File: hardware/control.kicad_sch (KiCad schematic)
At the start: 9 parts

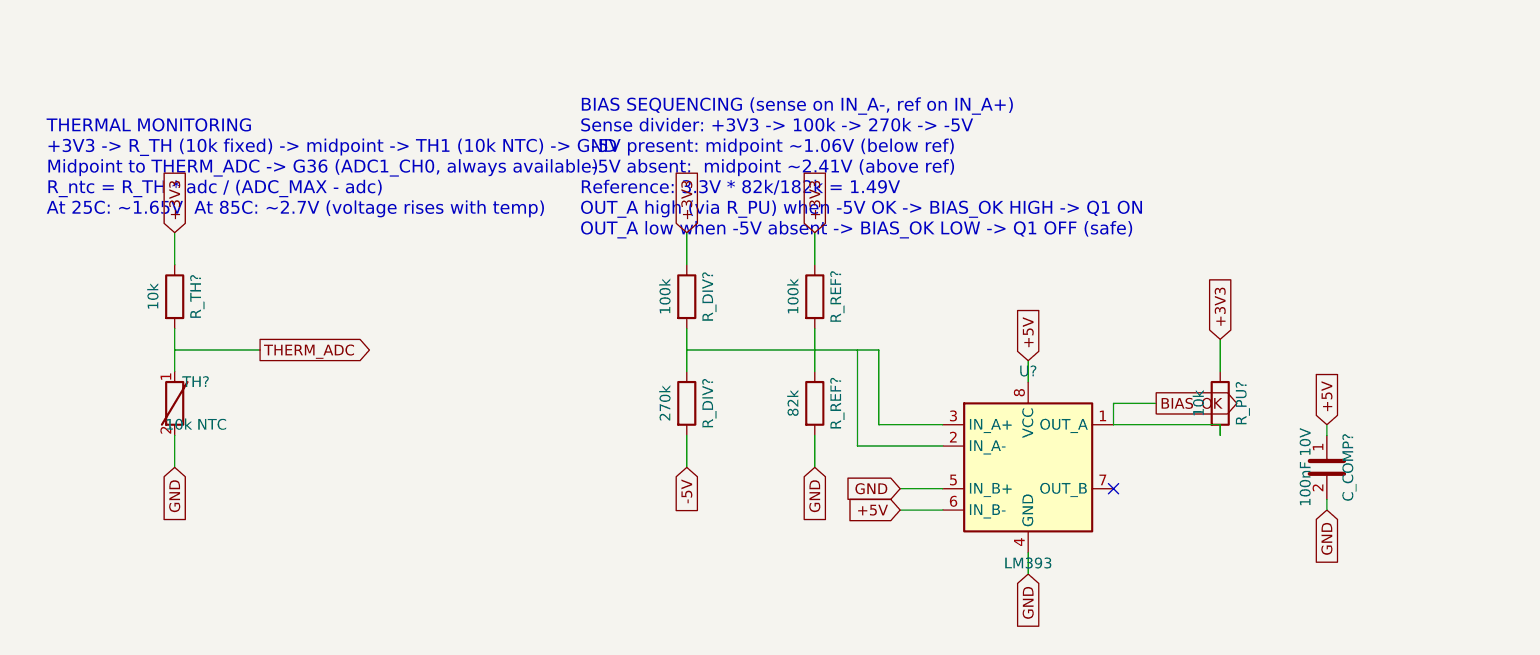
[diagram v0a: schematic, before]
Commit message: jamrf-v2: Add U3V70F15 WiFi PA regulator, FR408HR stackup, full firmware, custom footprints
- Add U3V70F15 buck-boost converter to limit WiFi PA supply to 15V (fixes ZVE-3W-83+ overvoltage)
- Update PCB stackup to Isola FR408HR (Er=3.65, tan d=0.0095) with corrected 0.40mm 50-ohm traces
- Add full operational firmware (main.py): chaos modulation engine, ST7789 display, mode control
- Add 6 custom footprints: M5StickC, Pololu D24V10F5/U3V70F15, Mini-Circuits, Wurth shield, isolator
- Add fp-lib-table and sym-lib-table for custom libraries
- Update README with logo, badges, TIIUAE disclaimer, corrected specs
- Update LICENSE with proper attribution

Co-Authored-By: Claude Opus 4.6 <noreply@anthropic.com>
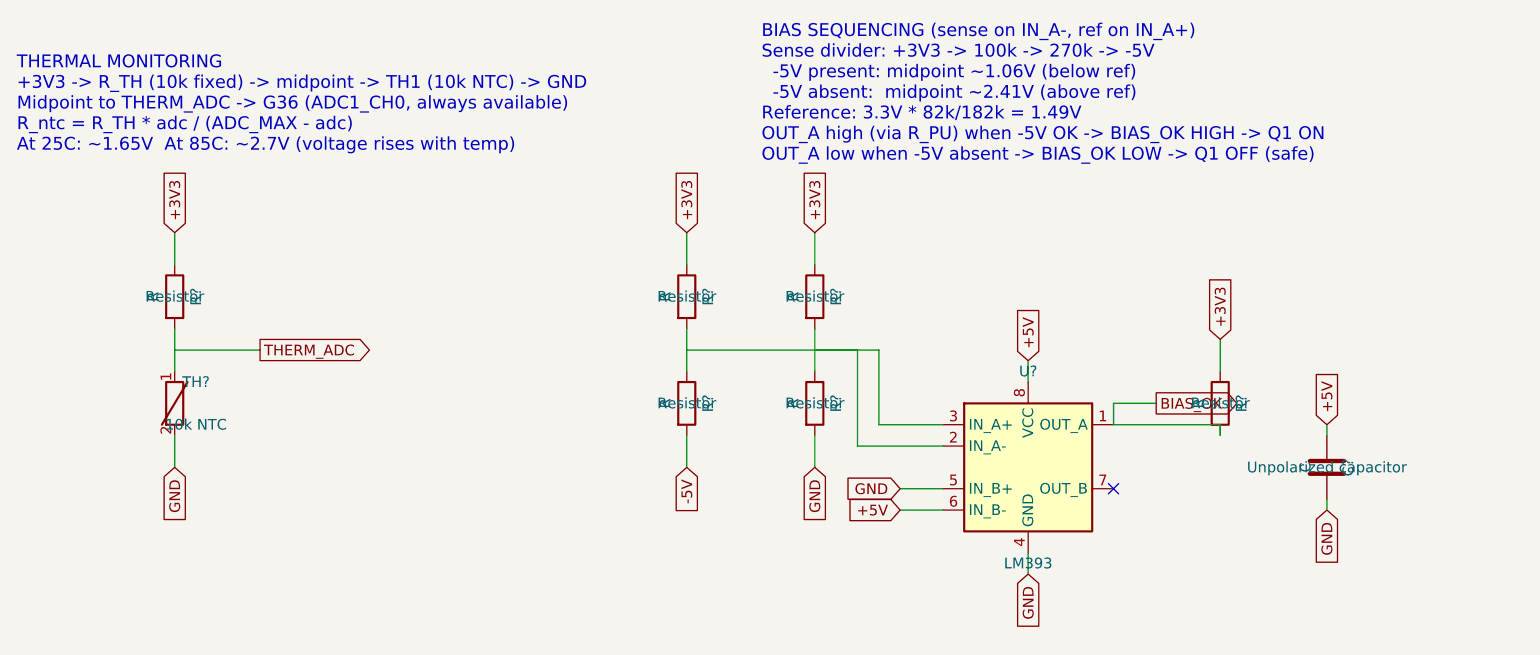
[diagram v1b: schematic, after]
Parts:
- C?: renamed from C_COMP?; value 100nF 10V -> C
- R?: renamed from R_TH?; value 10k -> R
- R?: renamed from R_DIV?; value 100k -> R
- R?: renamed from R_DIV?; value 270k -> R
- R?: renamed from R_REF?; value 100k -> R
- R?: renamed from R_REF?; value 82k -> R
- R?: renamed from R_PU?; value 10k -> R
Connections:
- net at U?.2 (IN_A-): now also R?.1, R?.1, R?.2, R?.2, U?.3 (IN_A+)
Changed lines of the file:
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@@
 	(text "THERMAL MONITORING\n+3V3 -> R_TH (10k fixed) -> midpoint -> TH1 (10k NTC) -> GND\nMidpoint to THERM_ADC -> G36 (ADC1_CH0, always available)\nR_ntc = R_TH * adc / (ADC_MAX - adc)\nAt 25C: ~1.65V  At 85C: ~2.7V (voltage rises with temp)"
 		(exclude_from_sim no)
-		(at 43.18 40.64 0)
+		(at 39.624 33.02 0)
 		(effects
 			(font
@@
 	(text "BIAS SEQUENCING (sense on IN_A-, ref on IN_A+)\nSense divider: +3V3 -> 100k -> 270k -> -5V\n  -5V present: midpoint ~1.06V (below ref)\n  -5V absent:  midpoint ~2.41V (above ref)\nReference: 3.3V * 82k/182k = 1.49V\nOUT_A high (via R_PU) when -5V OK -> BIAS_OK HIGH -> Q1 ON\nOUT_A low when -5V absent -> BIAS_OK LOW -> Q1 OFF (safe)"
 		(exclude_from_sim no)
-		(at 106.68 40.64 0)
+		(at 128.27 31.75 0)
 		(effects
 			(font
@@
 			)
 			(justify left)
-		)
-	)
-	(wire
-		(pts
-			(xy 149.86 78.74) (xy 144.78 78.74)
-		)
-		(stroke
-			(width 0)
-			(type default)
-		)
-	)
-	(wire
-		(pts
-			(xy 149.86 81.28) (xy 144.78 81.28)
-		)
-		(stroke
-			(width 0)
-			(type default)
-		)
-	)
-	(global_label "GND"
-		(shape input)
-		(at 144.78 78.74 180)
-		(effects
-			(font
-				(size 1.27 1.27)
-			)
-			(justify right)
-		)
-		(property "Intersheetrefs" "${INTERSHEET_REFS}"
-			(at 144.78 78.74 0)
-			(effects
-				(font
-					(size 1.27 1.27)
-				)
-				(hide yes)
-			)
-		)
-	)
-	(global_label "+5V"
-		(shape input)
-		(at 144.78 81.28 180)
-		(effects
-			(font
-				(size 1.27 1.27)
-			)
-			(justify right)
-		)
-		(property "Intersheetrefs" "${INTERSHEET_REFS}"
-			(at 144.78 81.28 0)
-			(effects
-				(font
-					(size 1.27 1.27)
-				)
-				(hide yes)
-			)
 		)
 	)
@@
 	(wire
 		(pts
-			(xy 119.38 62.23) (xy 142.24 62.23)
+			(xy 119.38 62.23) (xy 139.7 62.23)
+		)
+		(stroke
+			(width 0)
+			(type default)
+		)
+	)
+	(wire
+		(pts
+			(xy 134.62 62.23) (xy 142.24 62.23)
 		)
 		(stroke
@@
 		(pts
 			(xy 160.02 86.36) (xy 160.02 88.9)
+		)
+		(stroke
+			(width 0)
+			(type default)
+		)
+	)
+	(wire
+		(pts
+			(xy 149.86 78.74) (xy 144.78 78.74)
+		)
+		(stroke
+			(width 0)
+			(type default)
+		)
+	)
+	(wire
+		(pts
+			(xy 149.86 81.28) (xy 144.78 81.28)
+		)
+		(stroke
+			(width 0)
+			(type default)
+		)
+	)
+	(wire
+		(pts
+			(xy 195.58 71.12) (xy 195.58 72.39)
+		)
+		(stroke
+			(width 0)
+			(type default)
+		)
+	)
+	(wire
+		(pts
+			(xy 195.58 80.01) (xy 195.58 81.28)
 		)
 		(stroke
@@
 		(property "Intersheetrefs" "${INTERSHEET_REFS}"
 			(at 182.88 60.96 0)
+			(effects
+				(font
+					(size 1.27 1.27)
+				)
+				(hide yes)
+			)
+		)
+	)
+	(global_label "GND"
+		(shape input)
+		(at 144.78 78.74 180)
+		(effects
+			(font
+				(size 1.27 1.27)
+			)
+			(justify right)
+		)
+		(property "Intersheetrefs" "${INTERSHEET_REFS}"
+			(at 144.78 78.74 0)
+			(effects
+				(font
+					(size 1.27 1.27)
+				)
+				(hide yes)
+			)
+		)
+	)
+	(global_label "+5V"
+		(shape input)
+		(at 144.78 81.28 180)
+		(effects
+			(font
+				(size 1.27 1.27)
+			)
+			(justify right)
+		)
+		(property "Intersheetrefs" "${INTERSHEET_REFS}"
+			(at 144.78 81.28 0)
+			(effects
+				(font
+					(size 1.27 1.27)
+				)
+				(hide yes)
+			)
+		)
+	)
+	(global_label "+5V"
+		(shape input)
+		(at 195.58 71.12 90)
+		(effects
+			(font
+				(size 1.27 1.27)
+			)
+			(justify left)
+		)
+		(property "Intersheetrefs" "${INTERSHEET_REFS}"
+			(at 195.58 71.12 0)
+			(effects
+				(font
+					(size 1.27 1.27)
+				)
+				(hide yes)
+			)
+		)
+	)
+	(global_label "GND"
+		(shape input)
+		(at 195.58 81.28 270)
+		(effects
+			(font
+				(size 1.27 1.27)
+			)
+			(justify right)
+		)
+		(property "Intersheetrefs" "${INTERSHEET_REFS}"
+			(at 195.58 81.28 0)
 			(effects
 				(font
@@
 		(on_board yes)
 		(dnp no)
-		(property "Reference" "R_TH?"
+		(property "Reference" "R?"
 			(at 60.96 55.88 90)
 			(effects
@@
 			)
 		)
-		(property "Value" "10k"
+		(property "Value" "R"
 			(at 55.88 55.88 90)
 			(effects
@@
 			)
 		)
-		(property "Description" ""
+		(property "Description" "Resistor"
 			(at 58.42 55.88 0)
 			(effects
@@
 			(project "jamrf-v2"
 				(path "/b0000001-0000-0000-0000-000000000001/b0000001-0000-0000-0000-000000000050"
-					(reference "R_TH?")
+					(reference "R?")
 					(unit 1)
 				)
@@
 		(on_board yes)
 		(dnp no)
-		(property "Reference" "R_DIV?"
+		(property "Reference" "R?"
 			(at 121.92 55.88 90)
 			(effects
@@
 			)
 		)
-		(property "Value" "100k"
+		(property "Value" "R"
 			(at 116.84 55.88 90)
 			(effects
@@
 			)
 		)
-		(property "Description" ""
+		(property "Description" "Resistor"
 			(at 119.38 55.88 0)
 			(effects
@@
 			(project "jamrf-v2"
 				(path "/b0000001-0000-0000-0000-000000000001/b0000001-0000-0000-0000-000000000050"
-					(reference "R_DIV?")
+					(reference "R?")
 					(unit 1)
 				)
@@
 		(on_board yes)
 		(dnp no)
-		(property "Reference" "R_DIV?"
+		(property "Reference" "R?"
 			(at 121.92 68.58 90)
 			(effects
@@
 			)
 		)
-		(property "Value" "270k"
+		(property "Value" "R"
 			(at 116.84 68.58 90)
 			(effects
@@
 			)
 		)
-		(property "Description" ""
+		(property "Description" "Resistor"
 			(at 119.38 68.58 0)
 			(effects
@@
 			(project "jamrf-v2"
 				(path "/b0000001-0000-0000-0000-000000000001/b0000001-0000-0000-0000-000000000050"
-					(reference "R_DIV?")
+					(reference "R?")
 					(unit 1)
 				)
@@
 		(on_board yes)
 		(dnp no)
-		(property "Reference" "R_REF?"
+		(property "Reference" "R?"
 			(at 137.16 55.88 90)
 			(effects
@@
 			)
 		)
-		(property "Value" "100k"
+		(property "Value" "R"
 			(at 132.08 55.88 90)
 			(effects
@@
 			)
 		)
-		(property "Description" ""
+		(property "Description" "Resistor"
 			(at 134.62 55.88 0)
 			(effects
@@
 			(project "jamrf-v2"
 				(path "/b0000001-0000-0000-0000-000000000001/b0000001-0000-0000-0000-000000000050"
-					(reference "R_REF?")
+					(reference "R?")
 					(unit 1)
 				)
@@
 		(on_board yes)
 		(dnp no)
-		(property "Reference" "R_REF?"
+		(property "Reference" "R?"
 			(at 137.16 68.58 90)
 			(effects
@@
 			)
 		)
-		(property "Value" "82k"
+		(property "Value" "R"
 			(at 132.08 68.58 90)
 			(effects
@@
 			)
 		)
-		(property "Description" ""
+		(property "Description" "Resistor"
 			(at 134.62 68.58 0)
 			(effects
@@
 			(project "jamrf-v2"
 				(path "/b0000001-0000-0000-0000-000000000001/b0000001-0000-0000-0000-000000000050"
-					(reference "R_REF?")
+					(reference "R?")
 					(unit 1)
 				)
@@
 		(on_board yes)
 		(dnp no)
-		(property "Reference" "R_PU?"
+		(property "Reference" "R?"
 			(at 185.42 68.58 90)
 			(effects
@@
 			)
 		)
-		(property "Value" "10k"
+		(property "Value" "R"
 			(at 180.34 68.58 90)
 			(effects
@@
 			)
 		)
-		(property "Description" ""
+		(property "Description" "Resistor"
 			(at 182.88 68.58 0)
 			(effects
@@
 			(project "jamrf-v2"
 				(path "/b0000001-0000-0000-0000-000000000001/b0000001-0000-0000-0000-000000000050"
-					(reference "R_PU?")
+					(reference "R?")
 					(unit 1)
 				)
-			)
-		)
-	)
-	(wire
-		(pts
-			(xy 195.58 71.12) (xy 195.58 72.39)
-		)
-		(stroke
-			(width 0)
-			(type default)
-		)
-	)
-	(wire
-		(pts
-			(xy 195.58 80.01) (xy 195.58 81.28)
-		)
-		(stroke
-			(width 0)
-			(type default)
-		)
-	)
-	(global_label "+5V"
-		(shape input)
-		(at 195.58 71.12 90)
-		(effects
-			(font
-				(size 1.27 1.27)
-			)
-			(justify left)
-		)
-		(property "Intersheetrefs" "${INTERSHEET_REFS}"
-			(at 195.58 71.12 0)
-			(effects
-				(font
-					(size 1.27 1.27)
-				)
-				(hide yes)
-			)
-		)
-	)
-	(global_label "GND"
-		(shape input)
-		(at 195.58 81.28 270)
-		(effects
-			(font
-				(size 1.27 1.27)
-			)
-			(justify right)
-		)
-		(property "Intersheetrefs" "${INTERSHEET_REFS}"
-			(at 195.58 81.28 0)
-			(effects
-				(font
-					(size 1.27 1.27)
-				)
-				(hide yes)
 			)
 		)
@@
 		(on_board yes)
 		(dnp no)
-		(property "Reference" "C_COMP?"
+		(property "Reference" "C?"
 			(at 198.12 76.2 90)
 			(effects
@@
 			)
 		)
-		(property "Value" "100nF 10V"
+		(property "Value" "C"
 			(at 193.04 76.2 90)
 			(effects
@@
 			)
 		)
-		(property "Description" ""
+		(property "Description" "Unpolarized capacitor"
 			(at 195.58 76.2 0)
 			(effects
@@
 			(project "jamrf-v2"
 				(path "/b0000001-0000-0000-0000-000000000001/b0000001-0000-0000-0000-000000000050"
-					(reference "C_COMP?")
+					(reference "C?")
 					(unit 1)
 				)

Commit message: Annotate all component references and update CLAUDE.md
- All component references annotated (U1-U10, R1-R17, C1-C19, Q1-Q4, etc.)
- Fix CLAUDE.md: correct jamrf-v4 description (dual-band, not WiFi-only)
- Update CLAUDE.md: file paths match main branch structure, add firmware docs
- Remove resolved known issues (annotation, footprint library)

Co-Authored-By: Claude Opus 4.6 <noreply@anthropic.com>
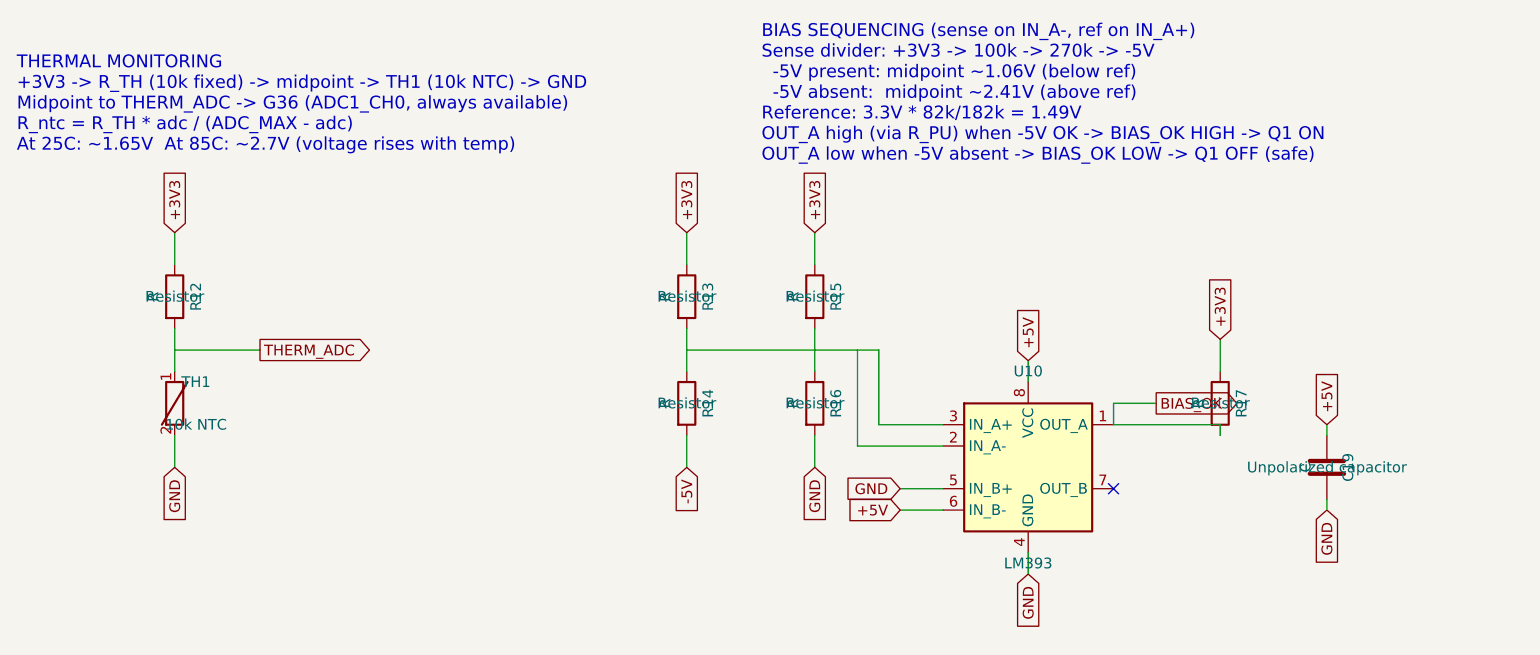
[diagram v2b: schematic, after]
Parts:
- gave numbers to parts that had none: 9
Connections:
- net at R13.2, R14.1, U10.3 (IN_A+): no longer R15.2, R16.1, U10.2 (IN_A-)
- new net: R15.2, R16.1
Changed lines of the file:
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@@
 	(wire
 		(pts
-			(xy 119.38 62.23) (xy 139.7 62.23)
-		)
-		(stroke
-			(width 0)
-			(type default)
-		)
-	)
-	(wire
-		(pts
-			(xy 134.62 62.23) (xy 142.24 62.23)
+			(xy 119.38 62.23) (xy 142.24 62.23)
 		)
 		(stroke
@@
 		(on_board yes)
 		(dnp no)
-		(property "Reference" "R?"
+		(property "Reference" "R12"
 			(at 60.96 55.88 90)
 			(effects
@@
 			(project "jamrf-v2"
 				(path "/b0000001-0000-0000-0000-000000000001/b0000001-0000-0000-0000-000000000050"
-					(reference "R?")
+					(reference "R12")
 					(unit 1)
 				)
@@
 		(on_board yes)
 		(dnp no)
-		(property "Reference" "TH?"
+		(property "Reference" "TH1"
 			(at 60.96 66.04 0)
 			(effects
@@
 			(project "jamrf-v2"
 				(path "/b0000001-0000-0000-0000-000000000001/b0000001-0000-0000-0000-000000000050"
-					(reference "TH?")
+					(reference "TH1")
 					(unit 1)
 				)
@@
 		(on_board yes)
 		(dnp no)
-		(property "Reference" "U?"
+		(property "Reference" "U10"
 			(at 160.02 64.77 0)
 			(effects
@@
 			(project "jamrf-v2"
 				(path "/b0000001-0000-0000-0000-000000000001/b0000001-0000-0000-0000-000000000050"
-					(reference "U?")
+					(reference "U10")
 					(unit 1)
 				)
@@
 		(on_board yes)
 		(dnp no)
-		(property "Reference" "R?"
+		(property "Reference" "R13"
 			(at 121.92 55.88 90)
 			(effects
@@
 			(project "jamrf-v2"
 				(path "/b0000001-0000-0000-0000-000000000001/b0000001-0000-0000-0000-000000000050"
-					(reference "R?")
+					(reference "R13")
 					(unit 1)
 				)
@@
 		(on_board yes)
 		(dnp no)
-		(property "Reference" "R?"
+		(property "Reference" "R14"
 			(at 121.92 68.58 90)
 			(effects
@@
 			(project "jamrf-v2"
 				(path "/b0000001-0000-0000-0000-000000000001/b0000001-0000-0000-0000-000000000050"
-					(reference "R?")
+					(reference "R14")
 					(unit 1)
 				)
@@
 		(on_board yes)
 		(dnp no)
-		(property "Reference" "R?"
+		(property "Reference" "R15"
 			(at 137.16 55.88 90)
 			(effects
@@
 			(project "jamrf-v2"
 				(path "/b0000001-0000-0000-0000-000000000001/b0000001-0000-0000-0000-000000000050"
-					(reference "R?")
+					(reference "R15")
 					(unit 1)
 				)
@@
 		(on_board yes)
 		(dnp no)
-		(property "Reference" "R?"
+		(property "Reference" "R16"
 			(at 137.16 68.58 90)
 			(effects
@@
 			(project "jamrf-v2"
 				(path "/b0000001-0000-0000-0000-000000000001/b0000001-0000-0000-0000-000000000050"
-					(reference "R?")
+					(reference "R16")
 					(unit 1)
 				)
@@
 		(on_board yes)
 		(dnp no)
-		(property "Reference" "R?"
+		(property "Reference" "R17"
 			(at 185.42 68.58 90)
 			(effects
@@
 			(project "jamrf-v2"
 				(path "/b0000001-0000-0000-0000-000000000001/b0000001-0000-0000-0000-000000000050"
-					(reference "R?")
+					(reference "R17")
 					(unit 1)
 				)
@@
 		(on_board yes)
 		(dnp no)
-		(property "Reference" "C?"
+		(property "Reference" "C19"
 			(at 198.12 76.2 90)
 			(effects
@@
 			(project "jamrf-v2"
 				(path "/b0000001-0000-0000-0000-000000000001/b0000001-0000-0000-0000-000000000050"
-					(reference "C?")
+					(reference "C19")
 					(unit 1)
 				)
